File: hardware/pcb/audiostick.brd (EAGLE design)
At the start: 84 x 34 mm, 65 parts, among them IC1 TPS73633MBDV, IC3 PCM5102ASW, IC5 AP22804W5, IC6 TINY13V-10SSU, J1 AVRISP6TH127, J2 AUDIO_JACK_3.5MM_PTH, J3 USB-B, SW1 EVQP7

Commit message: Final revision before manufacture
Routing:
- net GND: track 18.9 -> 6.27 mm
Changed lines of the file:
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@@
 <via x="30" y="23" extent="1-16" drill="0.254"/>
 <via x="28" y="23" extent="1-16" drill="0.254"/>
-<wire x1="31.9178" y1="14.725" x2="30" y2="14.725" width="0.3048" layer="1"/>
 <wire x1="30" y1="14.725" x2="29.275" y2="14.725" width="0.3048" layer="1"/>
 <wire x1="29.275" y1="14.725" x2="29" y2="15" width="0.3048" layer="1"/>
@@
 <contactref element="C13" pad="2"/>
 <contactref element="R10" pad="1"/>
-<wire x1="27.275" y1="14.725" x2="26.0822" y2="14.725" width="0.3048" layer="1"/>
-<wire x1="27.925" y1="14.075" x2="26.0822" y2="14.075" width="0.3048" layer="1"/>
 <contactref element="IC5" pad="2"/>
 <contactref element="C17" pad="2"/>
@@
 <contactref element="IC3" pad="11"/>
 <contactref element="IC3" pad="16"/>
-<wire x1="31.9178" y1="14.075" x2="31.075" y2="14.075" width="0.3048" layer="1"/>
-<wire x1="31.9178" y1="14.075" x2="30" y2="14.075" width="0.3048" layer="1"/>
 <wire x1="30" y1="14.075" x2="30" y2="14.725" width="0.3048" layer="1"/>
-<wire x1="25" y1="19.125" x2="25" y2="19" width="0.3048" layer="1"/>
-<wire x1="26.0822" y1="14.075" x2="29" y2="14.075" width="0.3048" layer="1"/>
 <wire x1="29" y1="14.075" x2="29" y2="15" width="0.3048" layer="1"/>
-<wire x1="31.9178" y1="17.325" x2="30" y2="17.325" width="0.3048" layer="1"/>
 <wire x1="30" y1="17.325" x2="30" y2="16" width="0.3048" layer="1"/>
 <contactref element="TP8" pad="TP"/>

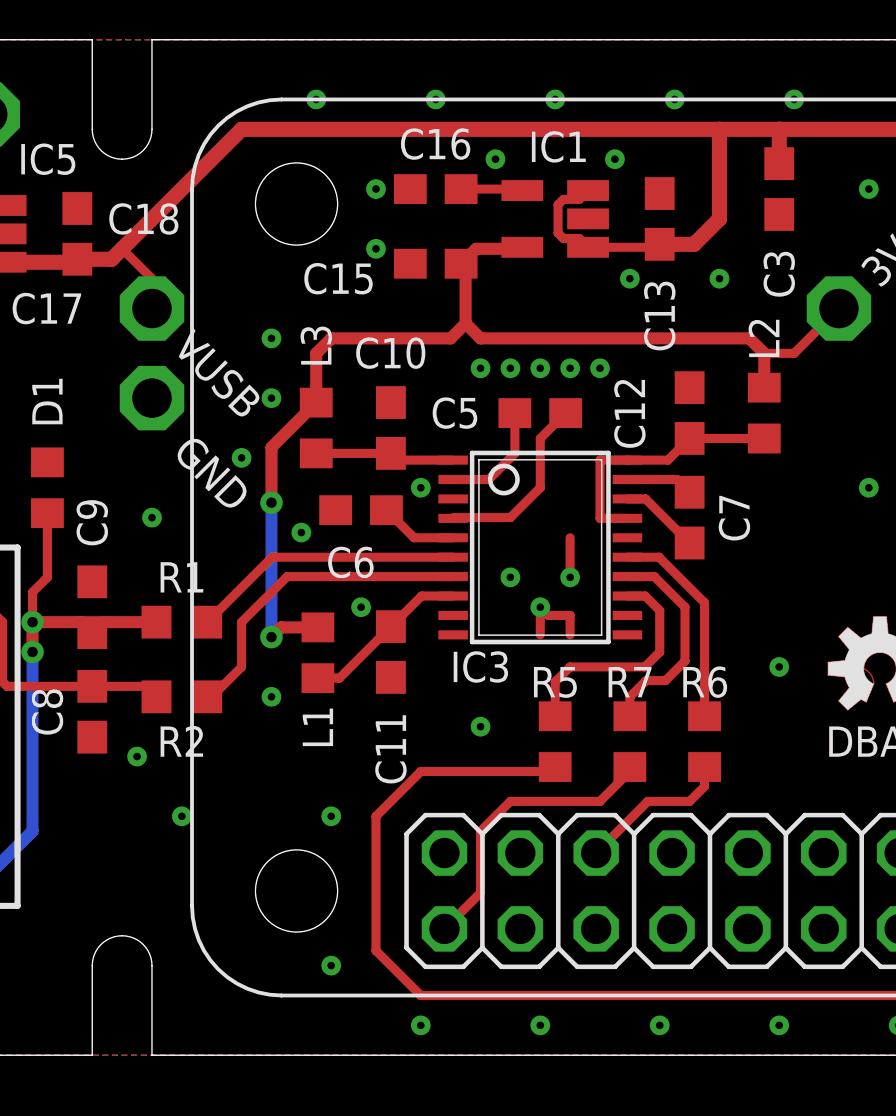
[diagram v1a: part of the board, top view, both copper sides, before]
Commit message: Moved vias for standoffs
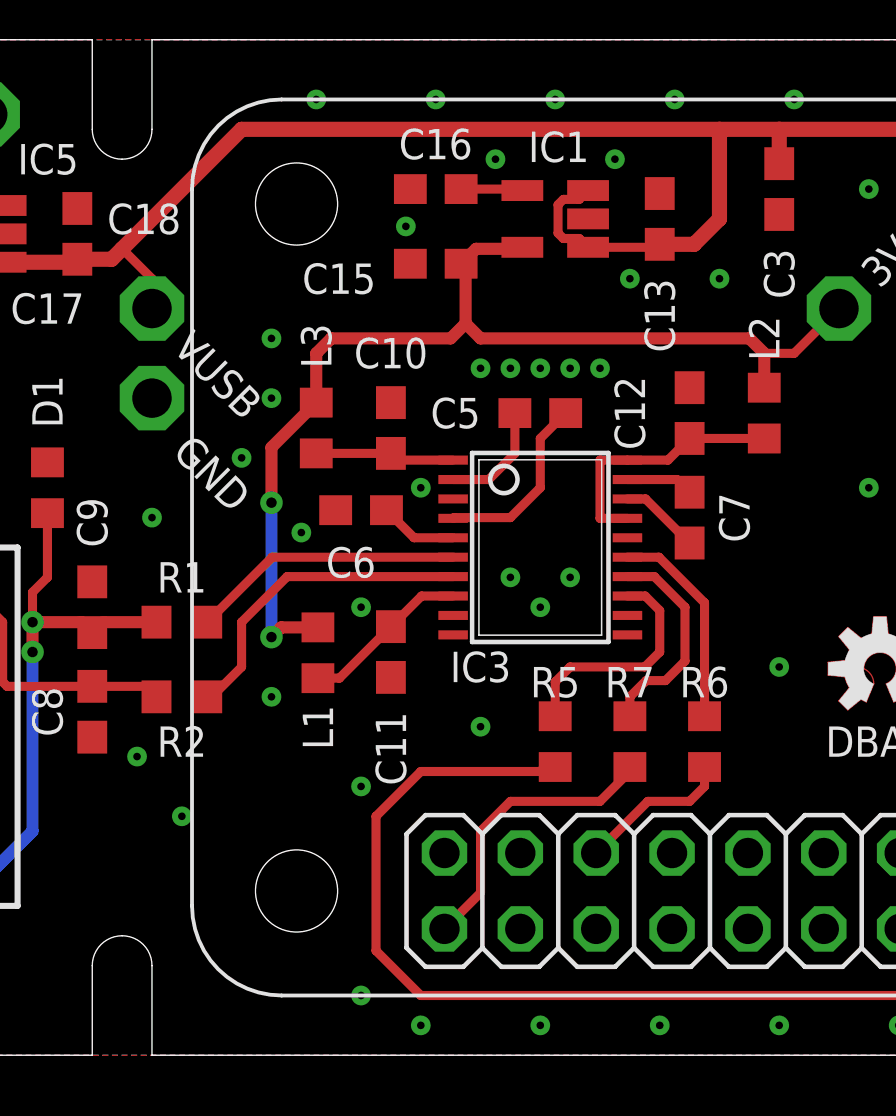
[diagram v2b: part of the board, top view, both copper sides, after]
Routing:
- net GND: track 6.27 -> 2.26 mm, vias 65 -> 64
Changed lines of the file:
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@@
 <via x="30" y="23" extent="1-16" drill="0.254"/>
 <via x="28" y="23" extent="1-16" drill="0.254"/>
-<wire x1="30" y1="14.725" x2="29.275" y2="14.725" width="0.3048" layer="1"/>
-<wire x1="29.275" y1="14.725" x2="29" y2="15" width="0.3048" layer="1"/>
 <contactref element="Q2" pad="5"/>
 <contactref element="C15" pad="2"/>
@@
 <contactref element="IC3" pad="11"/>
 <contactref element="IC3" pad="16"/>
-<wire x1="30" y1="14.075" x2="30" y2="14.725" width="0.3048" layer="1"/>
-<wire x1="29" y1="14.075" x2="29" y2="15" width="0.3048" layer="1"/>
-<wire x1="30" y1="17.325" x2="30" y2="16" width="0.3048" layer="1"/>
 <contactref element="TP8" pad="TP"/>
 <contactref element="TP9" pad="TP"/>
@@
 <via x="27" y="11" extent="1-16" drill="0.254"/>
 <via x="37" y="13" extent="1-16" drill="0.254"/>
-<via x="22" y="8" extent="1-16" drill="0.254"/>
-<via x="22" y="3" extent="1-16" drill="0.254"/>
+<via x="23" y="9" extent="1-16" drill="0.254"/>
+<via x="23" y="2" extent="1-16" drill="0.254"/>
 <via x="20" y="12" extent="1-16" drill="0.254"/>
 <contactref element="C3" pad="2"/>
@@
 <via x="35" y="26" extent="1-16" drill="0.254"/>
 <via x="32" y="26" extent="1-16" drill="0.254"/>
-<via x="23.5" y="29" extent="1-16" drill="0.254"/>
-<via x="23.5" y="27" extent="1-16" drill="0.254"/>
+<via x="24.5" y="27.75" extent="1-16" drill="0.254"/>
 <via x="20" y="24" extent="1-16" drill="0.254"/>
 <via x="20" y="22" extent="1-16" drill="0.254"/>

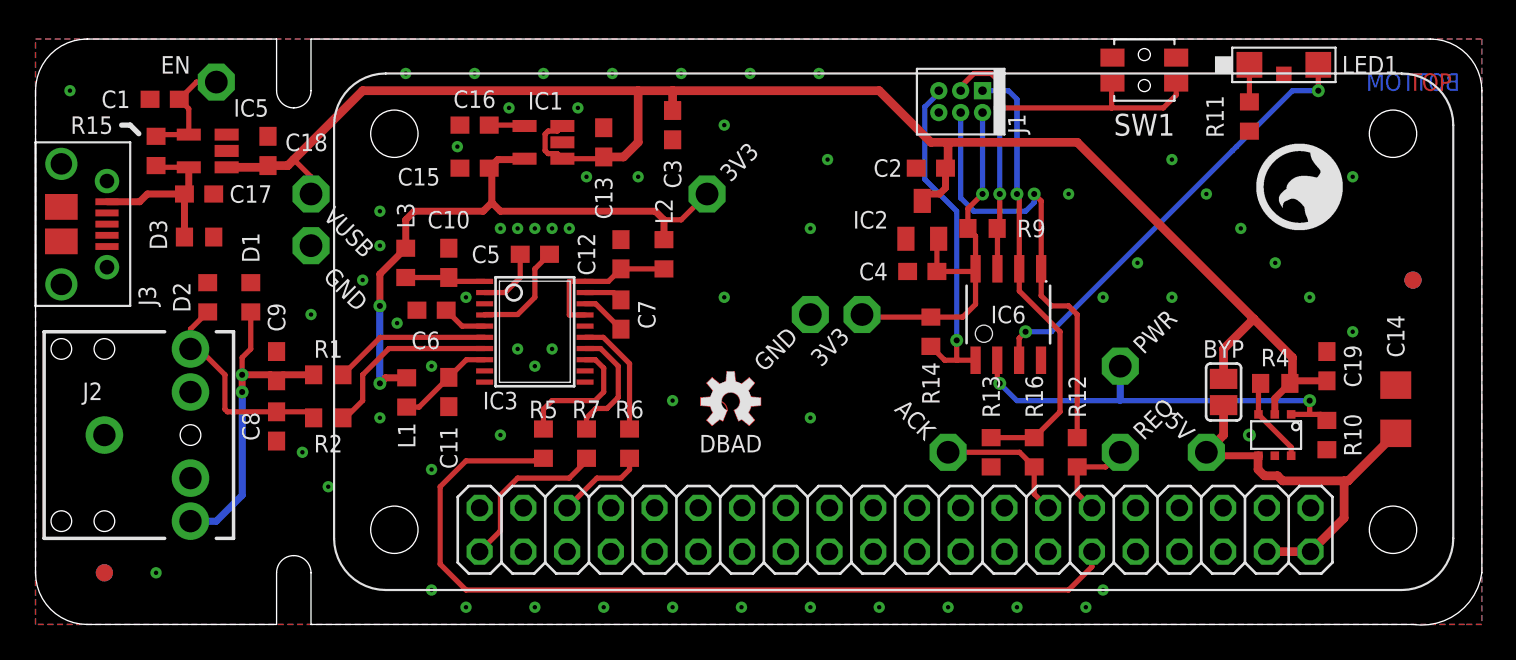
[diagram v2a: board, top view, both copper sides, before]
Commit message: 2.0 -> 2.1 simplification, PCB rearrangement
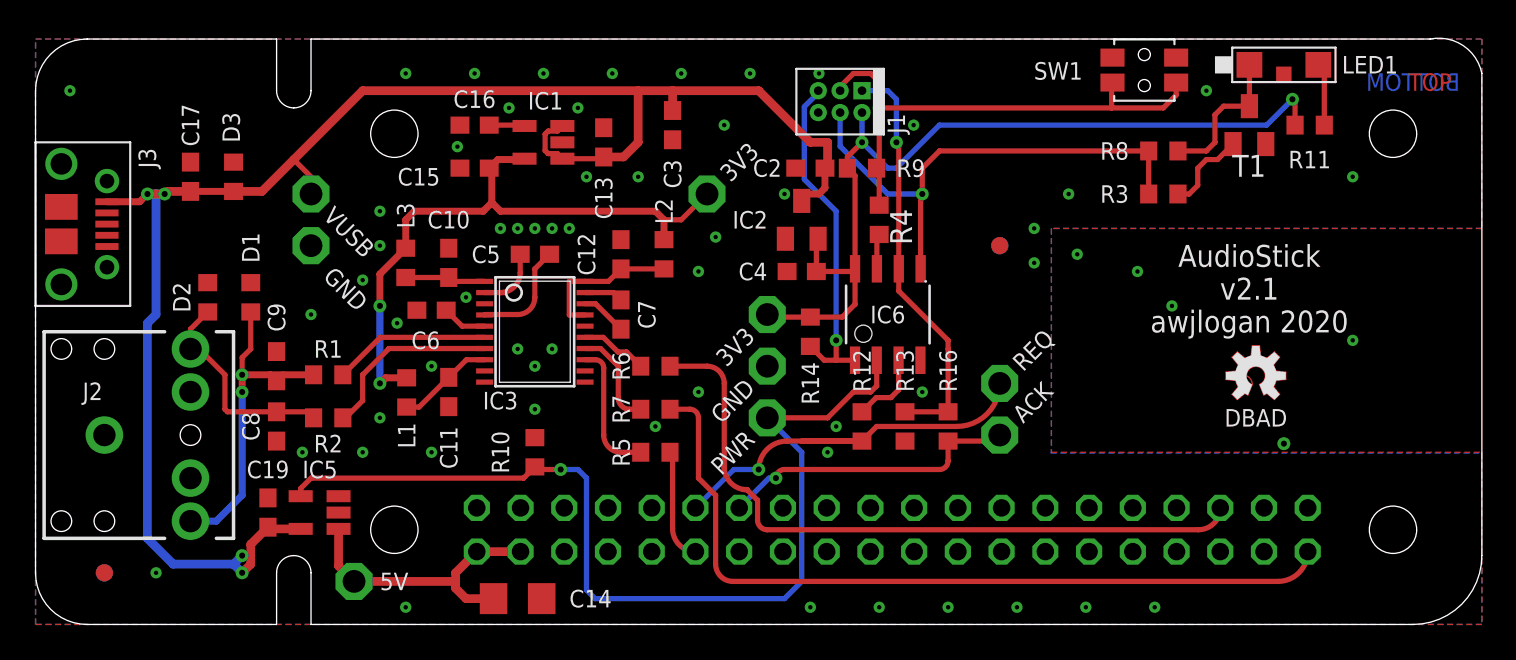
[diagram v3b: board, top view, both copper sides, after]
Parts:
- removed C1, C18: 100n, rcl:C0603
- removed Q2: (no value), AWJLEagleLib:6TSOP
- removed R15: 100K, rcl:R0603
- removed SJ1: (no value), jumper:SJ
- removed TP10: PTR1PAD1-13, testpad:P1-13
- removed U$2: (no value), logo:CS-2016-LOGO-5MM
- added R3: 10K, rcl:R0603
- added R8: 0R, rcl:R0603
- added T1: BC850, transistor:SOT23
- R4: value 100K -> 180R
- moved U$1 65.0 mm to (17.3, 32.0), flipped to the bottom
- moved C19 62.1 mm to (13.5, 6.50)
- moved C14 52.2 mm to (28.0, 1.50), turned to 0 degrees
- moved TP3 50.1 mm to (18.5, 2.50)
- moved R10 46.0 mm to (29.0, 10.0), turned to 270 degrees
- moved R4 24.9 mm to (49.0, 23.5), turned to 270 degrees
- moved F2 24.1 mm to (56.0, 22.0)
- moved IC5 22.0 mm to (16.5, 6.50)
- moved TP11 20.7 mm to (42.5, 12.0)
- moved R12 12.6 mm to (48.0, 11.5)
- moved TP5 8.06 mm to (56.0, 14.0)
- moved R9 7.83 mm to (48.0, 26.5)
- moved C2 7.00 mm to (45.0, 26.5)
- moved C4 7.00 mm to (44.5, 20.5)
- moved IC2 7.00 mm to (44.5, 23.5)
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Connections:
- removed net IN_EN: C1.1, IC5.4, R15.1, TP10.TP
- removed net V+: C17.1, D3.2, IC5.5, J3.VBUS, R15.2
- new net N$17: LED1.A, R11.1
- new net N$18: IC6.7, R4.2
- net +3V3: now also R11.2
- net +5V: now also C17.1, D3.2, IC5.5, J3.VBUS; no longer C18.1, IC5.1, Q2.2, R4.1, SJ1.2
- net +5V/1: now also IC5.1; no longer Q2.4, SJ1.1
- net GND: now also T1.2; no longer C1.2, C18.2, Q2.5, R11.1
- net LED: now also IC6.5, J1.4, R3.2, R8.2; no longer IC6.3, LED1.A
- net N$15: now also R8.1, T1.3; no longer R11.2
- net N$6: now also R3.1, T1.1; no longer Q2.3, Q2.6, R4.2
- net PWR: now also IC5.4; no longer Q2.1
- net REQ: now also IC6.3; no longer IC6.5, J1.4
- net SW: now also R4.1; no longer IC6.7
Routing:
- net BCK: track 51.1 -> 6.38 mm
- net DIN: track 9.75 -> 46.3 mm
- net LRCK: track 5.20 -> 40.4 mm
- net PWR: track 24.8 -> 56.4 mm, vias 2 -> 1
- net +3V3: track 22.9 -> 50.2 mm, vias 1 -> 2
- net REQ: track 26.0 -> 4.37 mm, vias 1 -> 0
- net S_REQ': track 5.58 -> 24.7 mm, vias 0 -> 1
- net V+: track 10.8 -> 0.00 mm
- net ACK_IN: track 8.07 -> 17.6 mm, vias 0 -> 1
- net +5V/1: track 23.9 -> 16.9 mm
- net IN_EN: track 6.78 -> 0.00 mm
- net N$15: track 2.15 -> 8.56 mm
- net LED: track 26.1 -> 30.0 mm, vias 2 -> 1
- net N$17: track 0.00 -> 3.64 mm
- net SW: track 26.7 -> 30.1 mm, vias 2 -> 1
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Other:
- outline, holes or cut-outs redrawn
- board text added: "AudioStick v2.1 awjlogan 2020"
- board text removed: "AudioStick v2.0 awjlogan 2020"
- board text removed: "BYP"
- board text removed: "EN"

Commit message: Change switch
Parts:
- removed SW1: EVQP7, AudioStick:EVQP7L
- added S1: (no value), switch-omron:B3F-31XX
- C14: value 47u -> 2u2; device rcl:C1206 -> rcl:C0805
- moved R3 4.03 mm to (69.5, 24.5), turned to 270 degrees
- moved R8 3.35 mm to (67.0, 24.5), turned to 270 degrees
- moved C14 1.50 mm to (26.5, 1.50)
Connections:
- net GND: now also S1.1; no longer SW1.2A, SW1.2B
- net SW: now also S1.2; no longer SW1.1A, SW1.1B
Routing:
- net SW: track 30.1 -> 22.7 mm
- net N$6: track 4.99 -> 2.57 mm
- net LED: track 30.0 -> 31.0 mm
- net N$15: track 8.56 -> 9.48 mm
- net +5V/1: track 16.9 -> 16.2 mm
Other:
- outline, holes or cut-outs redrawn
